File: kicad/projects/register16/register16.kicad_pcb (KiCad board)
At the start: 2 copper layers, 0 parts

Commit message: Steal libraries from ir pc project. Add template for CPU boards. Add readme. Very early stages of 16 bit register.
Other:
- rule via_min_size: 0.6 -> 0.4
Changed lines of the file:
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@@
     (via_size 0.8)
     (via_drill 0.4)
-    (via_min_size 0.6)
+    (via_min_size 0.4)
     (via_min_drill 0.3)
     (uvia_size 0.3)
@@
     (solder_mask_min_width 0.25)
     (aux_axis_origin 0 0)
-    (visible_elements 7FFFFFFF)
+    (visible_elements FFFFFF7F)
     (pcbplotparams
       (layerselection 0x010fc_ffffffff)

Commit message: Footprint association and initial component layout.
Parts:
- added C1: C, Capacitor_THT:C_Disc_D4.3mm_W1.9mm_P5.00mm, F.Cu at (78.5, 47.8)
- added C2: C, Capacitor_THT:C_Disc_D4.3mm_W1.9mm_P5.00mm, F.Cu at (125.4, 102.4)
- added C3: C, Capacitor_THT:C_Disc_D4.3mm_W1.9mm_P5.00mm, F.Cu at (162.4, 101.8)
- added C4: C, Capacitor_THT:C_Disc_D4.3mm_W1.9mm_P5.00mm, F.Cu at (206.3, 99.6)
- added C5: C, Capacitor_THT:C_Disc_D4.3mm_W1.9mm_P5.00mm, F.Cu at (245.4, 101.0)
- added C6: C, Capacitor_THT:C_Disc_D4.3mm_W1.9mm_P5.00mm, F.Cu at (204.1, 70.3)
- added C7: C, Capacitor_THT:C_Disc_D4.3mm_W1.9mm_P5.00mm, F.Cu at (245.4, 71.2)
- added D1: LED, LED_THT:LED_D5.0mm_Horizontal_O3.81mm_Z3.0mm, F.Cu at (281.4, 52.5)
- added D10: LED, LED_THT:LED_D5.0mm_Horizontal_O3.81mm_Z3.0mm, F.Cu at (224.2, 52.5)
- added D11: LED, LED_THT:LED_D5.0mm_Horizontal_O3.81mm_Z3.0mm, F.Cu at (217.8, 52.5)
- added D12: LED, LED_THT:LED_D5.0mm_Horizontal_O3.81mm_Z3.0mm, F.Cu at (211.5, 52.5)
- added D13: LED, LED_THT:LED_D5.0mm_Horizontal_O3.81mm_Z3.0mm, F.Cu at (205.2, 52.5)
- added D14: LED, LED_THT:LED_D5.0mm_Horizontal_O3.81mm_Z3.0mm, F.Cu at (198.8, 52.5)
- added D15: LED, LED_THT:LED_D5.0mm_Horizontal_O3.81mm_Z3.0mm, F.Cu at (192.4, 52.5)
- added D16: LED, LED_THT:LED_D5.0mm_Horizontal_O3.81mm_Z3.0mm, F.Cu at (186.1, 52.5)
- added D2: LED, LED_THT:LED_D5.0mm_Horizontal_O3.81mm_Z3.0mm, F.Cu at (275.0, 52.5)
- added D3: LED, LED_THT:LED_D5.0mm_Horizontal_O3.81mm_Z3.0mm, F.Cu at (268.6, 52.5)
- added D4: LED, LED_THT:LED_D5.0mm_Horizontal_O3.81mm_Z3.0mm, F.Cu at (262.3, 52.5)
- added D5: LED, LED_THT:LED_D5.0mm_Horizontal_O3.81mm_Z3.0mm, F.Cu at (255.9, 52.5)
- added D6: LED, LED_THT:LED_D5.0mm_Horizontal_O3.81mm_Z3.0mm, F.Cu at (249.6, 52.5)
- added D7: LED, LED_THT:LED_D5.0mm_Horizontal_O3.81mm_Z3.0mm, F.Cu at (243.2, 52.5)
- added D8: LED, LED_THT:LED_D5.0mm_Horizontal_O3.81mm_Z3.0mm, F.Cu at (236.9, 52.5)
- added D9: LED, LED_THT:LED_D5.0mm_Horizontal_O3.81mm_Z3.0mm, F.Cu at (230.6, 52.5)
- added J1: INPUT_ENABLE, Connector_Wire:SolderWirePad_1x01_Drill1mm, F.Cu at (127.6, 88.4)
- added J10: LOW, Connector_Wire:SolderWirePad_1x01_Drill1mm, F.Cu at (189.6, 78.5)
- added J2: OUTPUT_ENABLE, Connector_Wire:SolderWirePad_1x01_Drill1mm, F.Cu at (177.4, 78.7)
- added J3: CONTENTS, Connector_PinSocket_2.54mm:PinSocket_1x16_P2.54mm_Horizontal, F.Cu at (158.8, 35.6)
- added J4: Control_signal_backplane, eight-bit-computer:backplane-connector, F.Cu at (287.2, 133.8)
- added J5: Aux_connection, Connector_PinHeader_2.54mm:PinHeader_1x10_P2.54mm_Horizontal, F.Cu at (131.6, 131.8)
- added J6: Bus_connection, Connector_PinHeader_2.54mm:PinHeader_1x16_P2.54mm_Horizontal, F.Cu at (188.4, 131.7)
- added J7: HIGH, Connector_Wire:SolderWirePad_1x01_Drill1mm, F.Cu at (138.1, 88.5)
- added J8: LOW, Connector_Wire:SolderWirePad_1x01_Drill1mm, F.Cu at (132.6, 88.3)
- added J9: HIGH, Connector_Wire:SolderWirePad_1x01_Drill1mm, F.Cu at (183.6, 78.4)
- added RN1: R_Network08_US, Resistor_THT:R_Array_SIP9, F.Cu at (273.6, 63.5)
- added RN2: R_Network08_US, Resistor_THT:R_Array_SIP9, F.Cu at (209.1, 63.7)
- added U1: 74HCT04, Package_DIP:DIP-14_W7.62mm_Socket, F.Cu at (82.6, 42.3)
- added U2: 74HCT377, Package_DIP:DIP-20_W7.62mm_Socket, F.Cu at (131.5, 108.8)
- added U3: 74HCT377, Package_DIP:DIP-20_W7.62mm_Socket, F.Cu at (167.9, 107.4)
- added U4: 74HCT245, Package_DIP:DIP-20_W7.62mm_Socket, F.Cu at (212.2, 106.0)
- added U5: 74HCT245, Package_DIP:DIP-20_W7.62mm_Socket, F.Cu at (251.4, 107.3)
- added U6: 74HCT245, Package_DIP:DIP-20_W7.62mm_Socket, F.Cu at (210.1, 76.6)
- added U7: 74HCT245, Package_DIP:DIP-20_W7.62mm_Socket, F.Cu at (251.3, 77.7)
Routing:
- net (no net): track 0.00 -> 430.8 mm, vias 0 -> 34
- net GND: track 0.00 -> 20.3 mm, vias 0 -> 2

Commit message: More pcblayout
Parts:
- moved J2 99.8 mm to (274.3, 102.5), turned to 270 degrees
- moved J9 96.0 mm to (274.7, 108.6), turned to 270 degrees
- moved J10 92.3 mm to (274.6, 114.7), turned to 270 degrees
- moved U1 80.4 mm to (96.5, 121.4), turned to 90 degrees
- moved C1 68.5 mm to (89.9, 115.3)
- moved J1 35.3 mm to (94.8, 101.6)
- moved J8 35.3 mm to (99.8, 101.5)
- moved J7 35.3 mm to (105.4, 101.7)
- moved J3 22.1 mm to (157.7, 57.7)
- moved C6 18.9 mm to (185.4, 73.7)
- moved J6 18.2 mm to (170.2, 132.1)
- moved C5 17.7 mm to (228.6, 106.6), turned to 90 degrees
- moved U6 17.7 mm to (193.0, 81.3)
- moved C4 17.3 mm to (190.5, 106.6), turned to 90 degrees
- moved U5 15.3 mm to (236.2, 109.2)
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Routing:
- net (no net): track 430.8 -> 0.00 mm, vias 34 -> 2
- net /CNT04: track 0.00 -> 117.6 mm
- net /CNT06: track 0.00 -> 117.6 mm, vias 0 -> 1
- net /CNT05: track 0.00 -> 117.6 mm, vias 0 -> 1
- net /CNT07: track 0.00 -> 117.4 mm, vias 0 -> 1
- net /CNT13: track 0.00 -> 117.1 mm
- net /CNT12: track 0.00 -> 117.1 mm
- net /CNT15: track 0.00 -> 117.1 mm
- net /CNT14: track 0.00 -> 117.1 mm
- net /CNT03: track 0.00 -> 109.5 mm
- net /CNT02: track 0.00 -> 109.5 mm, vias 0 -> 1
- net /CNT01: track 0.00 -> 109.5 mm, vias 0 -> 1
- net /CNT00: track 0.00 -> 109.2 mm, vias 0 -> 1
- net /CNT11: track 0.00 -> 109.0 mm
- net /CNT10: track 0.00 -> 109.0 mm
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
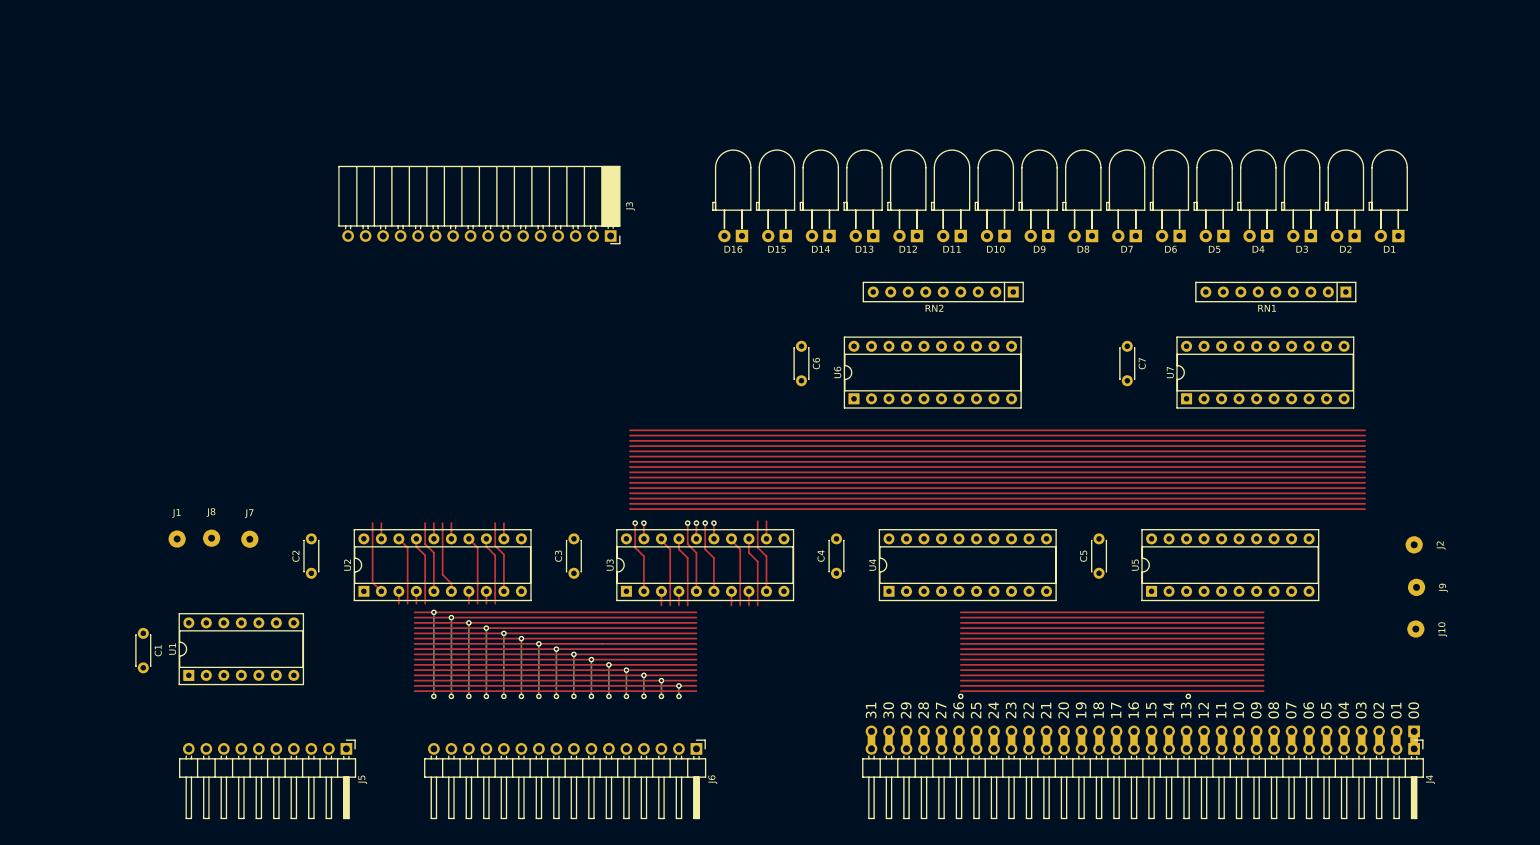
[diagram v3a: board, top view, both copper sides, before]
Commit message: More PCB layout for reg16. Almost at the point where it's time to start a bigger circuit to see what max board size will need to be.
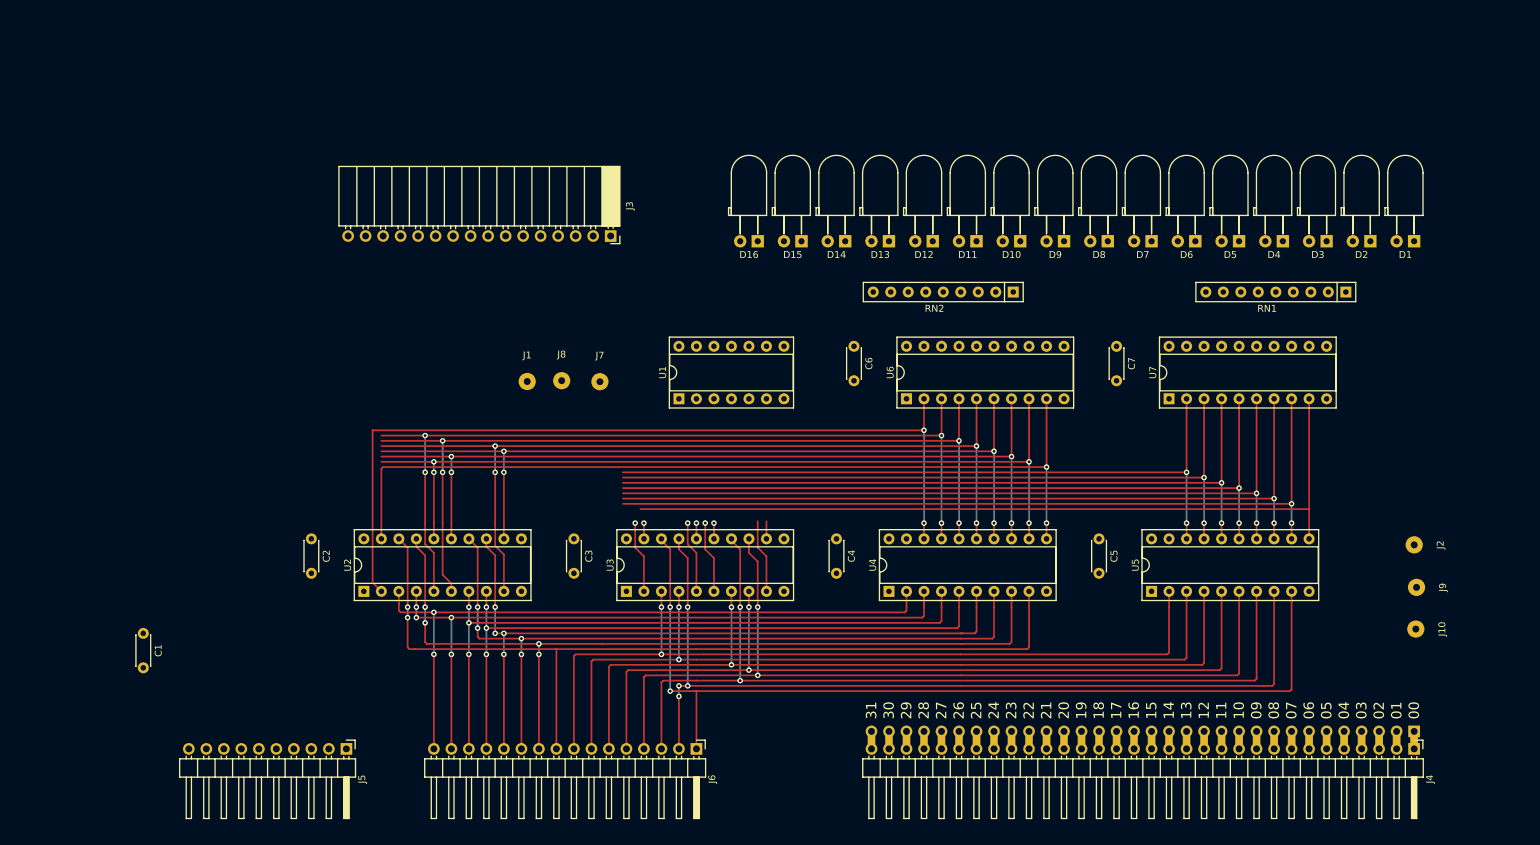
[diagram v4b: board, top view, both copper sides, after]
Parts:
- moved U1 81.7 mm to (167.6, 81.3)
- moved J7 55.7 mm to (156.2, 78.8)
- moved J1 55.7 mm to (145.6, 78.8)
- moved J8 55.7 mm to (150.6, 78.6)
- moved C6 7.62 mm to (193.0, 73.7)
- moved U6 7.62 mm to (200.7, 81.3)
- moved C2 5.00 mm to (114.3, 101.6), turned to 270 degrees
- moved C3 5.00 mm to (152.4, 101.6), turned to 270 degrees
- moved C4 5.00 mm to (190.5, 101.6), turned to 270 degrees
- moved C5 5.00 mm to (228.6, 101.6), turned to 270 degrees
- moved U7 2.54 mm to (238.8, 81.3)
- moved D1 2.41 mm to (274.3, 58.4)
- moved D10 2.41 mm to (217.2, 58.4)
- moved D11 2.41 mm to (210.8, 58.4)
- moved D12 2.41 mm to (204.5, 58.4)
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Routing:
- net /BUS00: track 94.8 -> 135.3 mm, vias 0 -> 2
- net /BUS01: track 96.3 -> 130.7 mm, vias 2 -> 4
- net /BUS02: track 97.0 -> 129.8 mm
- net /BUS03: track 97.8 -> 129.0 mm
- net /BUS04: track 90.4 -> 120.1 mm
- net /BUS05: track 91.2 -> 119.3 mm
- net /BUS08: track 101.6 -> 129.3 mm
- net /BUS06: track 91.9 -> 118.8 mm
- net /BUS07: track 92.7 -> 117.8 mm
- net /BUS09: track 102.4 -> 123.7 mm, vias 2 -> 4
- net /CNT08: track 109.0 -> 127.1 mm, vias 0 -> 2
- net /CNT09: track 109.0 -> 125.5 mm, vias 0 -> 4
- net /CNT10: track 109.0 -> 123.7 mm, vias 0 -> 4
- net /CNT11: track 109.0 -> 121.9 mm, vias 0 -> 4
- net /CNT12: track 117.1 -> 128.3 mm, vias 0 -> 4
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
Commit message: Got as far as I can with reg 16 PCB
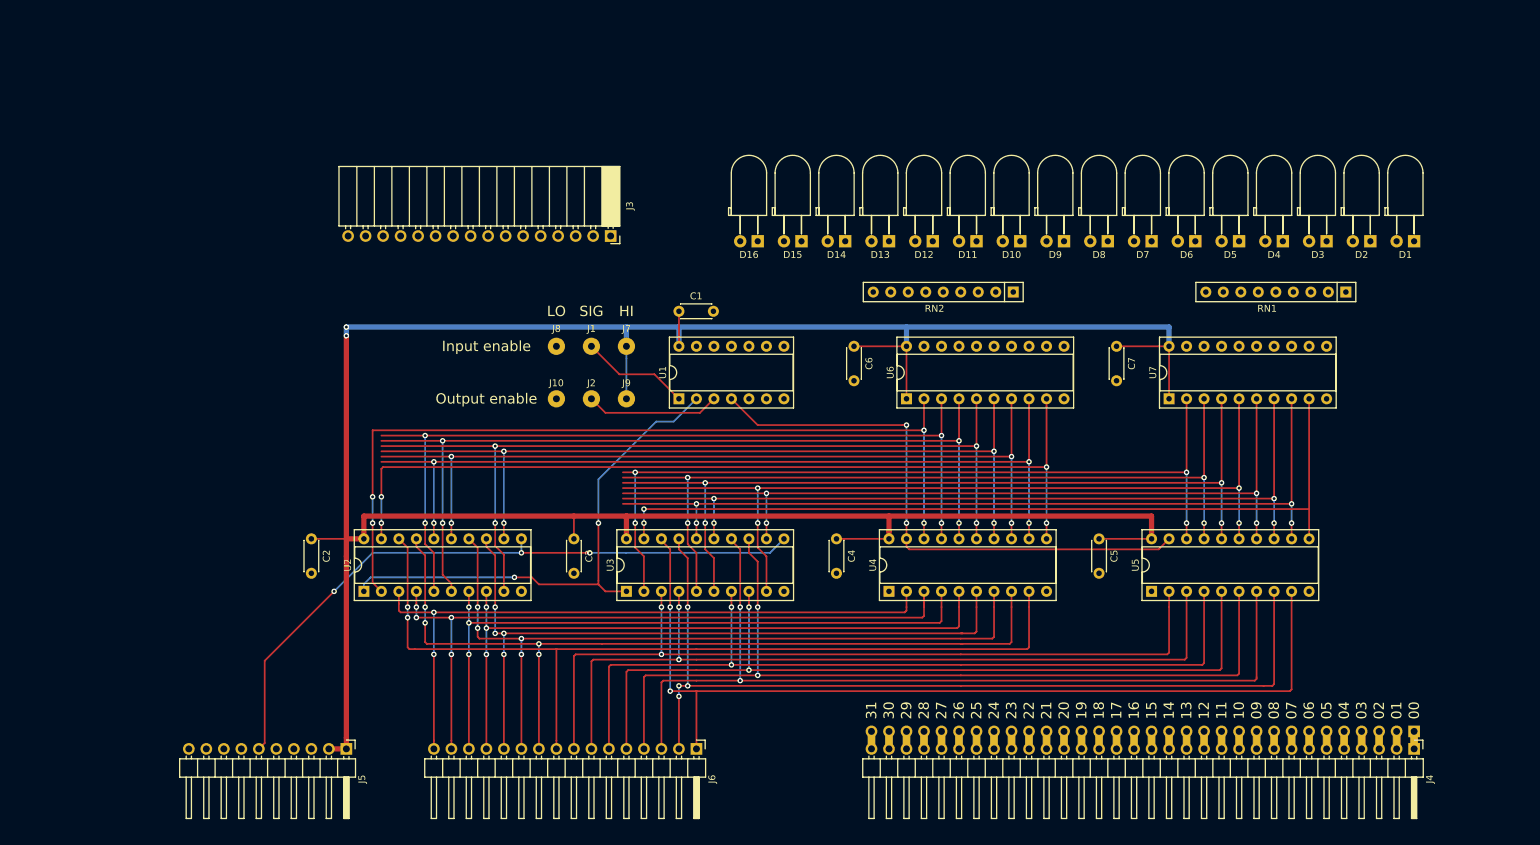
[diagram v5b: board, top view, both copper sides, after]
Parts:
- moved J10 129.1 mm to (149.9, 81.3), turned to 0 degrees
- moved J2 121.3 mm to (154.9, 81.3), turned to 0 degrees
- moved J9 117.9 mm to (160.0, 81.3), turned to 0 degrees
- moved C1 90.7 mm to (167.6, 68.6), turned to 0 degrees
- moved J1 10.6 mm to (154.9, 73.7)
- moved J7 6.42 mm to (160.0, 73.7)
- moved J8 5.05 mm to (149.9, 73.7)
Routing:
- net VCC: track 0.00 -> 391.2 mm, vias 0 -> 2
- net /DATA_CLK: track 0.00 -> 97.9 mm, vias 0 -> 3
- net Net-(U1-Pad4): track 0.00 -> 83.5 mm, vias 0 -> 2
- net Net-(U1-Pad2): track 0.00 -> 74.7 mm, vias 0 -> 2
- net Net-(J2-Pad1): track 0.00 -> 19.5 mm
- net Net-(J1-Pad1): track 0.00 -> 15.9 mm
- net /CNT07: track 112.5 -> 119.9 mm, vias 3 -> 4
- net /CNT06: track 115.6 -> 122.2 mm, vias 3 -> 4
- net /CNT05: track 118.1 -> 124.0 mm, vias 3 -> 4
- net /CNT04: track 120.7 -> 125.5 mm, vias 2 -> 4
- net /CNT03: track 115.1 -> 119.4 mm, vias 2 -> 4
- net /CNT02: track 117.6 -> 121.2 mm, vias 3 -> 4
- net /CNT01: track 120.1 -> 122.9 mm, vias 3 -> 4
- net /CNT00: track 119.9 -> 121.4 mm, vias 1 -> 2
- net /CNT15: vias 2 -> 4
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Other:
- board text added: "HI"
- board text added: "Input enable"
- board text added: "LO"
- board text added: "Output enable"
- board text added: "SIG"

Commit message: Register mostly complete
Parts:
- D1, D10, D11, D12, D13, D14, D15, D16, D2, D3, D4, D5, D6, D7, D8, D9: footprint LED_THT:LED_D5.0mm_Horizontal_O3.81mm_Z3.0mm -> eight-bit-computer:LED_D5.0mm_Horizontal_O3.81mm_Z3.0mm
- moved J1 115.7 mm to (264.2, 111.8)
- moved J2 115.7 mm to (264.2, 119.4)
- moved J7 115.7 mm to (269.2, 111.8)
- moved J8 115.7 mm to (259.1, 111.8)
- moved J9 115.7 mm to (269.2, 119.4)
- moved J10 115.7 mm to (259.1, 119.4)
- moved J3 44.4 mm to (114.3, 48.3)
- moved C1 13.0 mm to (154.9, 71.1), turned to 270 degrees
- moved D1 7.62 mm to (274.3, 50.8)
- moved D10 7.62 mm to (217.2, 50.8)
- moved D11 7.62 mm to (210.8, 50.8)
- moved D12 7.62 mm to (204.5, 50.8)
- moved D13 7.62 mm to (198.1, 50.8)
- moved D14 7.62 mm to (191.8, 50.8)
- moved D15 7.62 mm to (185.4, 50.8)
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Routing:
- net GND: track 0.00 -> 218.9 mm, vias 0 -> 2
- net Net-(J1-Pad1): track 15.9 -> 143.3 mm, vias 0 -> 3
- net Net-(J2-Pad1): track 19.5 -> 144.7 mm, vias 0 -> 3
- net /CNT07: track 119.9 -> 219.0 mm, vias 4 -> 6
- net /CNT06: track 122.2 -> 220.0 mm, vias 4 -> 6
- net /CNT05: track 124.0 -> 219.5 mm, vias 4 -> 6
- net /CNT04: track 125.5 -> 219.2 mm, vias 4 -> 6
- net /CNT03: track 119.4 -> 211.3 mm, vias 4 -> 6
- net /CNT02: track 121.2 -> 211.3 mm, vias 4 -> 6
- net /CNT00: track 121.4 -> 211.3 mm, vias 2 -> 6
- net /CNT01: track 122.9 -> 211.3 mm, vias 4 -> 6
- net /CNT15: track 124.2 -> 201.0 mm
- net /CNT14: track 124.8 -> 201.5 mm, vias 4 -> 6
- net /CNT13: track 126.5 -> 201.2 mm, vias 4 -> 6
- net /CNT12: track 128.3 -> 201.2 mm, vias 4 -> 6
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- added copper zone on B.Cu, net GND
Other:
- board outline added: 203.2 x 97.8 mm
- net class Default: clearance 0.1778 -> 0.2
- rule trace_clearance: 0.1778 -> 0.2
- board text added: "Contents"
- board text added: "JLCJLCJLCJLC"
- board text added: "REGISTER"
